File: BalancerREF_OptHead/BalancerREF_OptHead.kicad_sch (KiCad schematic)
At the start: 24 parts, among them J5 TO MAIN BOARD, Q1 AO3400A, U4 TS3021IYLT, U8 TLV9062IDR

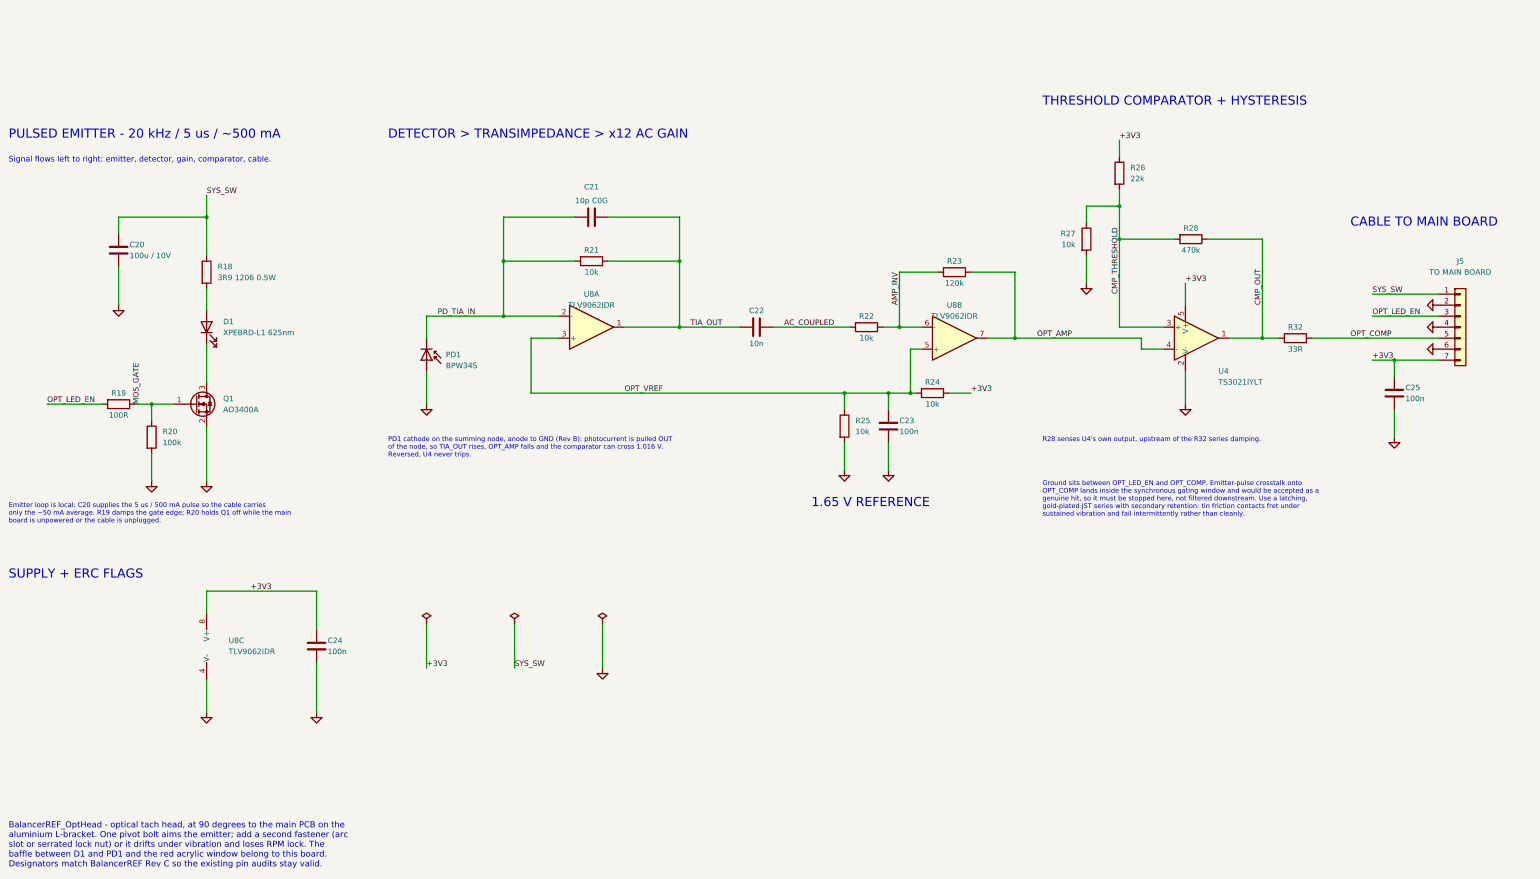
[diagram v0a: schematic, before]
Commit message: feat: BalancerCarrier on a FeatherS3[D], and two board fixes
Adds BalancerCarrier: the HOBOVibe instrument rebuilt as a carrier around an
Unexpected Maker FeatherS3[D] (ESP32-S3, 16 MB flash, 8 MB QSPI PSRAM), so the
MCU, LiPo charger, fuel gauge and USB come from a proven module instead of being
respun. 31 parts, ERC 0 violations.

The module is a Feather, so U1 uses Module:Adafruit_Feather-compatible geometry -
Unexpected Maker's own 28-pad footprint and symbol, checked pin-for-pin against
their FeatherS3[D] schematic headers J1 and JP3. That makes the footprint
vendor-independent: another Feather drops in without a respin, which is the
exposure that bit this project when the DFR0975 went pre-order only.

Seven parts came out once the module's own hardware was traced properly. LDO2
(NCP167BMX330TBG, 700 mA) is fed from VBUS, which ORs USB and VBAT, so it is live
on battery and powers the GPS - the discrete load switch went. The onboard
MAX17048 fuel gauge reads the cell directly over I2C, so the supply-sense divider
went with it.

Board fixes, both found by diffing against BalancerREF rather than trusting what
was drawn:

  BalancerREF  R30/C28 100k/1n -> 10k/10n. TI SCES586E section 5.8 characterises
               10k/10n at tw 100-110 us across all four supply voltages; 100k is
               ten times beyond the largest Rext TI characterises.

  OptHead      PD1 BPW34S -> SFH 2440. The old line was unbuildable: an SMD
               footprint against Vishay's BPW34S, which doc 81521 calls "leaded",
               naming an Osram part that is out of production. SFH 2440 is
               pad-identical, peaks at 620 nm against the 625 nm emitter, and
               blocks the IR the BPW34 was most sensitive to. C21 10 pF -> 22 pF:
               junction capacitance roughly doubles, so Cf_min rises to ~12.3 pF
               and the fitted 10 pF would peak. NOT SFH 2430 - 200 us rise time.

PhotoTach-BOM.csv rebuilt. It had nine classes of error, the worst struc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
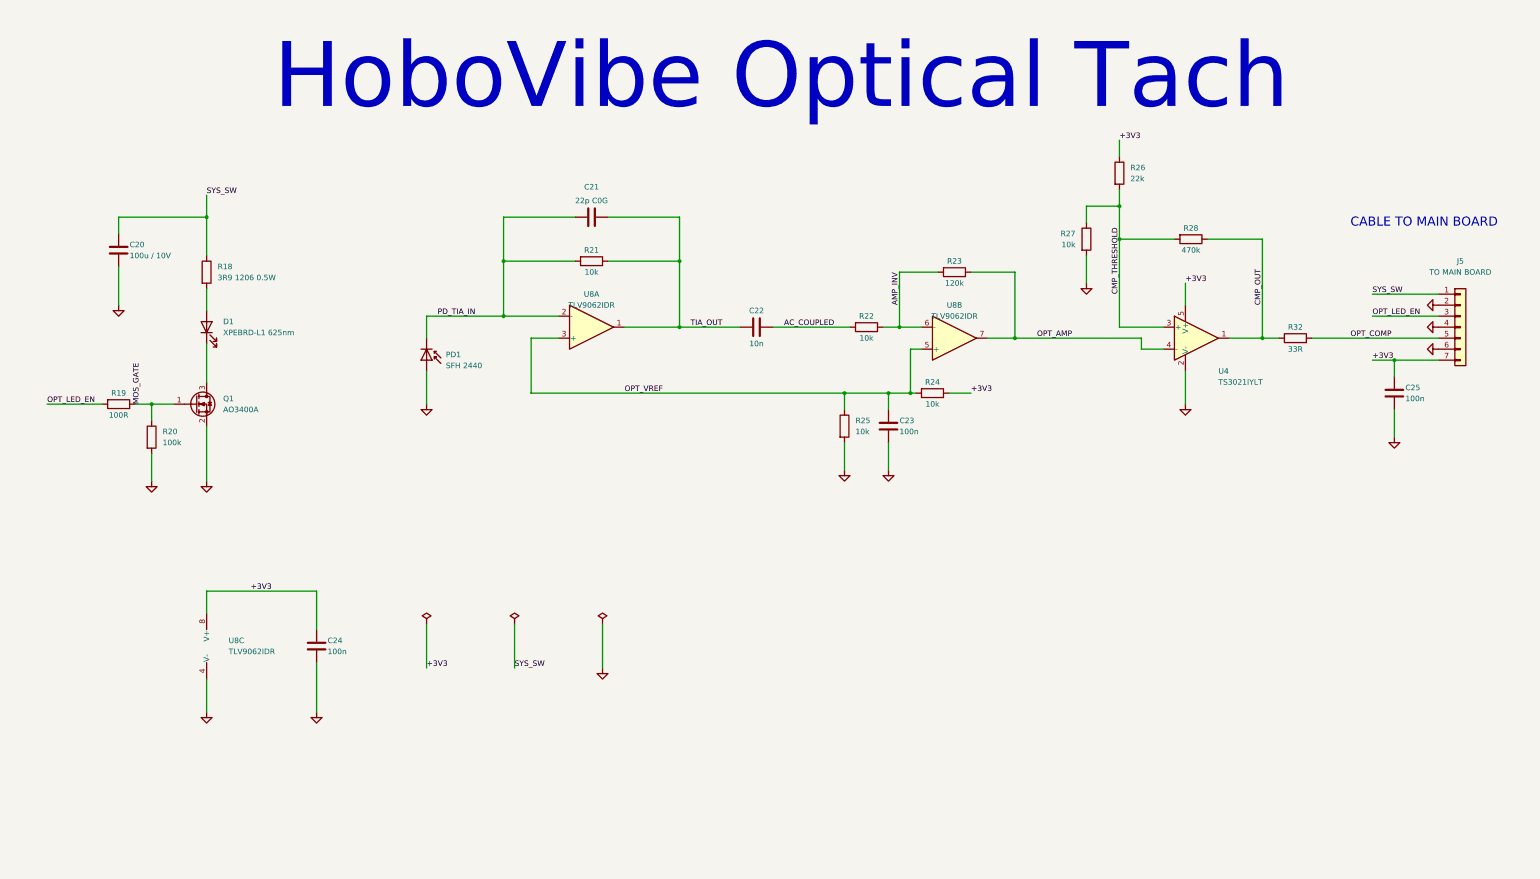
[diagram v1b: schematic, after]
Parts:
- C21: value 10p C0G -> 22p C0G; MPN 10p C0G -> 22p C0G
- PD1: value BPW34S -> SFH 2440; footprint OptoDevice:Osram_BPW34S-SMD -> OptoDevice:Osram_SFH2440; symbol Sensor_Optical:BPW34 -> Sensor_Optical:SFH2440; MPN BPW34S -> SFH 2440
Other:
- note added: "HoboVibe Optical Tach"
- note removed: "1.65 V REFERENCE"
- note removed: "BalancerREF_OptHead - optical tach head, at 90 degrees to the main PCB on the aluminium L-bracket. One pivot bolt aims the emitter; add a second fastener (arc slot or serrated lock nut) or it drifts under vibration and loses RPM lock. The baffle between D1 and PD1 and the red acrylic window belong to this board. Designators match BalancerREF Rev C so the existing pin audits stay valid."
- note removed: "DETECTOR > TRANSIMPEDANCE > x12 AC GAIN"
- note removed: "Emitter loop is local: C20 supplies the 5 us / 500 mA pulse so the cable carries only the ~50 mA average. R19 damps the gate edge; R20 holds Q1 off while the main board is unpowered or the cable is unplugged."
- note removed: "Ground sits between OPT_LED_EN and OPT_COMP. Emitter-pulse crosstalk onto OPT_COMP lands inside the synchronous gating window and would be accepted as a genuine hit, so it must be stopped here, not filtered downstream. Use a latching, gold-plated JST series with secondary retention: tin friction contacts fret under sustained vibration and fail intermittently rather than cleanly."
- note removed: "PD1 cathode on the summing node, anode to GND (Rev B): photocurrent is pulled OUT of the node, so TIA_OUT rises, OPT_AMP falls and the comparator can cross 1.016 V. Reversed, U4 never trips."
- note removed: "PULSED EMITTER - 20 kHz / 5 us / ~500 mA"
- note removed: "R28 senses U4's own output, upstream of the R32 series damping."
- note removed: "SUPPLY + ERC FLAGS"
- note removed: "Signal flows left to right: emitter, detector, gain, comparator, cable."
- note removed: "THRESHOLD COMPARATOR + HYSTERESIS"
- company: Split from BalancerREF Rev C -> (none)
- title: BalancerREF_OptHead - pivoting optical tach head -> Optical Tach Board
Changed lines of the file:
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@@
 	(paper "A3")
 	(title_block
-		(title "BalancerREF_OptHead - pivoting optical tach head")
+		(title "Optical Tach Board")
 		(date "2026-09-11")
 		(rev "B")
-		(company "Split from BalancerREF Rev C")
-		(comment 1 "Cable carries DC rails and digital edges only")
 	)
-	(text "Signal flows left to right: emitter, detector, gain, comparator, cable."
+	(text "HoboVibe Optical Tach"
 		(exclude_from_sim no)
-		(at 30.48 52.07 0)
+		(at 208.915 33.655 0)
 		(effects
 			(font
-				(size 1.3 1.3)
+				(size 15 15)
 			)
-			(justify left top)
-		)
-	)
-	(text "PULSED EMITTER - 20 kHz / 5 us / ~500 mA"
-		(exclude_from_sim no)
-		(at 30.48 45.72 0)
-		(effects
-			(font
-				(size 2.1 2.1)
-			)
-			(justify left top)
-		)
-	)
-	(text "Ground sits between OPT_LED_EN and OPT_COMP. Emitter-pulse crosstalk onto\nOPT_COMP lands inside the synchronous gating window and would be accepted as a\ngenuine hit, so it must be stopped here, not filtered downstream. Use a latching,\ngold-plated JST series with secondary retention: tin friction contacts fret under\nsustained vibration and fail intermittently rather than cleanly."
-		(exclude_from_sim no)
-		(at 269.24 127 0)
-		(effects
-			(font
-				(size 1.1 1.1)
-			)
-			(justify left top)
-		)
-	)
-	(text "PD1 cathode on the summing node, anode to GND (Rev B): photocurrent is pulled OUT\nof the node, so TIA_OUT rises, OPT_AMP falls and the comparator can cross 1.016 V.\nReversed, U4 never trips."
-		(exclude_from_sim no)
-		(at 118.11 116.84 0)
-		(effects
-			(font
-				(size 1.1 1.1)
-			)
-			(justify left top)
-		)
-	)
-	(text "1.65 V REFERENCE"
-		(exclude_from_sim no)
-		(at 215.9 130.81 0)
-		(effects
-			(font
-				(size 2.1 2.1)
-			)
-			(justify left top)
-		)
-	)
-	(text "SUPPLY + ERC FLAGS"
-		(exclude_from_sim no)
-		(at 30.48 147.32 0)
-		(effects
-			(font
-				(size 2.1 2.1)
-			)
-			(justify left top)
 		)
 	)
@@
 		)
 	)
-	(text "R28 senses U4's own output, upstream of the R32 series damping."
-		(exclude_from_sim no)
-		(at 269.24 116.84 0)
-		(effects
-			(font
-				(size 1.1 1.1)
-			)
-			(justify left top)
-		)
-	)
-	(text "BalancerREF_OptHead - optical tach head, at 90 degrees to the main PCB on the\naluminium L-bracket. One pivot bolt aims the emitter; add a second fastener (arc\nslot or serrated lock nut) or it drifts under vibration and loses RPM lock. The\nbaffle between D1 and PD1 and the red acrylic window belong to this board.\nDesignators match BalancerREF Rev C so the existing pin audits stay valid."
-		(exclude_from_sim no)
-		(at 30.48 205.74 0)
-		(effects
-			(font
-				(size 1.4 1.4)
-			)
-			(justify left top)
-		)
-	)
-	(text "Emitter loop is local: C20 supplies the 5 us / 500 mA pulse so the cable carries\nonly the ~50 mA average. R19 damps the gate edge; R20 holds Q1 off while the main\nboard is unpowered or the cable is unplugged."
-		(exclude_from_sim no)
-		(at 30.48 132.08 0)
-		(effects
-			(font
-				(size 1.1 1.1)
-			)
-			(justify left top)
-		)
-	)
-	(text "DETECTOR > TRANSIMPEDANCE > x12 AC GAIN"
-		(exclude_from_sim no)
-		(at 118.11 45.72 0)
-		(effects
-			(font
-				(size 2.1 2.1)
-			)
-			(justify left top)
-		)
-	)
-	(text "THRESHOLD COMPARATOR + HYSTERESIS"
-		(exclude_from_sim no)
-		(at 269.24 38.1 0)
-		(effects
-			(font
-				(size 2.1 2.1)
-			)
-			(justify left top)
-		)
-	)
 	(junction
 		(at 144.78 76.2)
@@
 			)
 		)
-		(property "Value" "10p C0G"
+		(property "Value" "22p C0G"
 			(at 165.1 62.23 90)
 			(show_name no)
@@
 			)
 		)
-		(property "MPN" "10p C0G"
+		(property "MPN" "22p C0G"
 			(at 165.1 63.5 90)
 			(hide yes)
@@
 	)
 	(symbol
-		(lib_id "Sensor_Optical:BPW34")
+		(lib_id "Sensor_Optical:SFH2440")
 		(at 127 99.06 270)
 		(unit 1)
@@
 			)
 		)
-		(property "Value" "BPW34S"
+		(property "Value" "SFH 2440"
 			(at 131.45 100.33 90)
 			(show_name no)
@@
 			)
 		)
-		(property "Footprint" "OptoDevice:Osram_BPW34S-SMD"
+		(property "Footprint" "OptoDevice:Osram_SFH2440"
 			(at 131.45 97.79 90)
 			(hide yes)
@@
 			)
 		)
-		(property "Datasheet" "http://www.vishay.com/docs/81521/bpw34.pdf"
+		(property "Datasheet" "https://look.ams-osram.com/m/68c5b1c5aa457db1/original/SFH-2440.pdf"
 			(at 131.45 97.79 90)
 			(hide yes)
@@
 			)
 		)
-		(property "MPN" "BPW34S"
+		(property "MPN" "SFH 2440"
 			(at 131.45 97.79 90)
 			(hide yes)

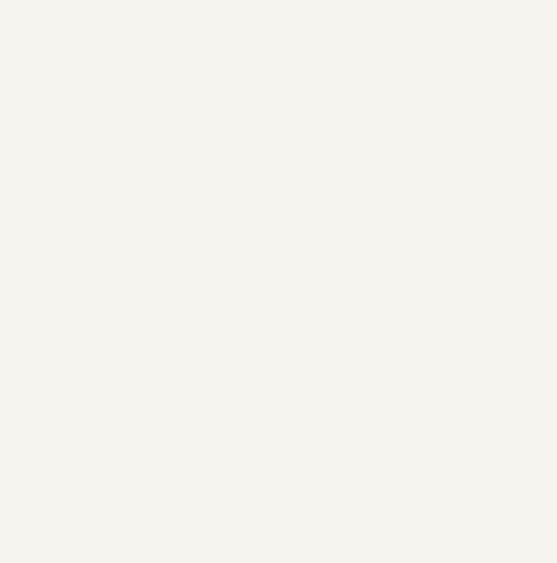
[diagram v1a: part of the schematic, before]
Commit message: feat: carrier PCB first layout, schematic fixes, OptHead 3D models
BalancerCarrier
  - First .kicad_pcb into git: 4 layers, 139 tracks, 51 vias, GND on In1.Cu
    and +3V3 on In2.Cu, 0 unconnected. Placement recovered from
    temp-freerouting.dsn after the Freerouting crash took the board file.
  - Schematic fixes found in review: LED1 was wired backwards (cathode on the
    GPIO), R13 sat in series with J5.5 instead of returning to GND, and
    GPS_UART_RX collided with the module I2C bus on IO9 - moved to IO7.
  - The GPS block is kept but DNP for the first round; the board is a
    proof-of-concept that the balancer works before the GPS is added on.
  - .kicad_pro carries the netclasses the board's DRC depends on, so it goes
    in with the board rather than after it.
  - scripts/restore_placement_pcbnew.py is the recovery tool that worked.
    restore_placement_from_dsn.py is kept beside it with a header explaining
    why editing the file directly shears the pads: KiCad stores each pad's
    angle including its parent footprint's.

BalancerREF_OptHead
  - PD1 is now an SFH 2440. The SFH 2430 it replaces has a 200 us rise time
    against the 2440's 0.09 us, which cannot resolve a rotor blade passing.
  - 3D models attached to D1 and PD1.

Known, not fixed here: 13 DRC violations on the carrier, 12 of them U5's LGA
pad-to-pad gap of 0.150 mm against the 0.2 mm netclass clearance (needs a
local override, not a layout change), and one benign J3 THT layer mismatch.
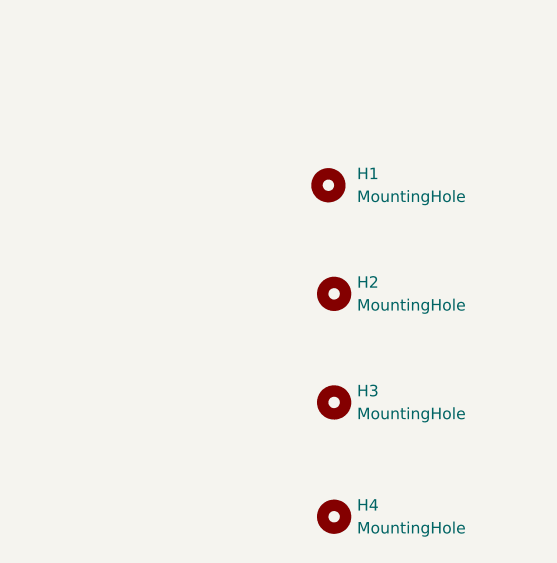
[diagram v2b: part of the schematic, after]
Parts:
- added H1, H2, H3, H4: MountingHole, MountingHole:MountingHole_2.2mm_M2_DIN965, symbol Mechanical:MountingHole
